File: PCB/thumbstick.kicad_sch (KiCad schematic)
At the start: 2 parts

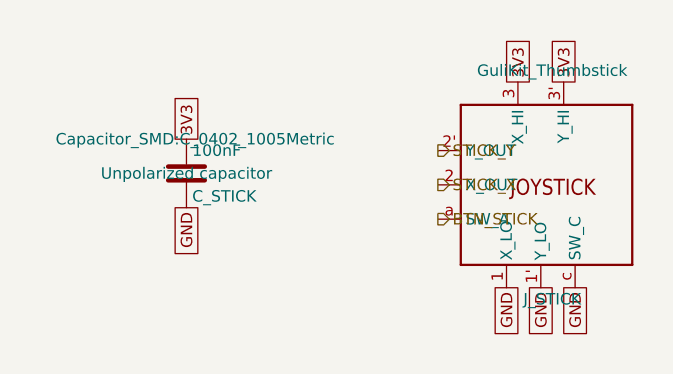
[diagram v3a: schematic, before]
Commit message: layout: everything is on the board
The board edge cuts are down to 100mm x 35mm. All the components have the right footprints and are on the board, but no traces exist yet, and not all circuits are laid out properly yet. Lots of DRC warnings.
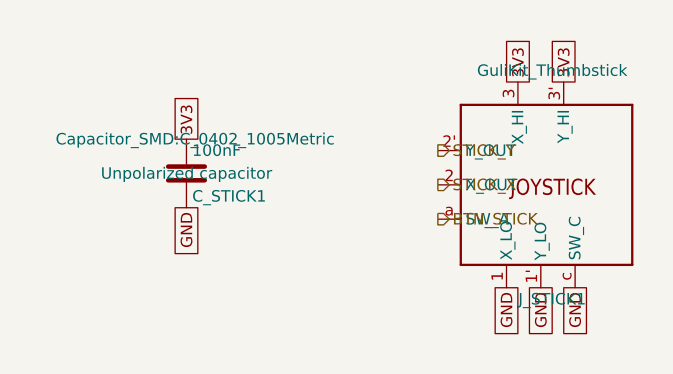
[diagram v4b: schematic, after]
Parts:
- removed C_STICK: 100nF, Capacitor_SMD:C_0402_1005Metric, symbol Device:C
- removed J_STICK: GuliKit_Thumbstick, SnipsControllers_Custom:GuliKit_HallStick, symbol SnipsControllers_Custom:GuliKit_HallStick
- added C_STICK1: 100nF, Capacitor_SMD:C_0402_1005Metric, symbol Device:C
- added J_STICK1: GuliKit_Thumbstick, SnipsControllers_Custom:GuliKit_HallStick, symbol SnipsControllers_Custom:GuliKit_HallStick
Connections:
- net 3V3: now also C_STICK1.1, J_STICK1.3 (X_HI), J_STICK1.3' (Y_HI)
- net BTN_STICK: now also J_STICK1.a (SW_A)
- net GND: now also C_STICK1.2, J_STICK1.1 (X_LO), J_STICK1.1' (Y_LO), J_STICK1.c (SW_C)
- net STICK_X: now also J_STICK1.2 (X_OUT)
- net STICK_Y: now also J_STICK1.2' (Y_OUT)
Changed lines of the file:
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@@
+		)
+	)
+	(global_label "3V3"
+		(shape passive)
+		(at 170.18 93.98 90)
+		(fields_autoplaced yes)
+		(effects
+			(font
+				(size 1.27 1.27)
+			)
+			(justify left)
+		)
+		(property "Intersheetrefs" "${INTERSHEET_REFS}"
+			(at 170.18 93.98 0)
+			(hide yes)
+			(show_name no)
+			(do_not_autoplace no)
+			(effects
+				(font
+					(size 1.27 1.27)
+				)
+			)
 		)
 	)
 	(global_label "GND"
 		(shape passive)
+		(at 163.83 116.84 270)
+		(fields_autoplaced yes)
+		(effects
+			(font
+				(size 1.27 1.27)
+			)
+			(justify right)
+		)
+		(property "Intersheetrefs" "${INTERSHEET_REFS}"
+			(at 163.83 116.84 0)
+			(hide yes)
+			(show_name no)
+			(do_not_autoplace no)
+			(effects
+				(font
+					(size 1.27 1.27)
+				)
+			)
+		)
+	)
+	(global_label "3V3"
+		(shape passive)
+		(at 128.27 100.33 90)
+		(fields_autoplaced yes)
+		(effects
+			(font
+				(size 1.27 1.27)
+			)
+			(justify left)
+		)
+		(property "Intersheetrefs" "${INTERSHEET_REFS}"
+			(at 128.27 100.33 0)
+			(hide yes)
+			(show_name no)
+			(do_not_autoplace no)
+			(effects
+				(font
+					(size 1.27 1.27)
+				)
+			)
+		)
+	)
+	(global_label "GND"
+		(shape passive)
 		(at 128.27 107.95 270)
 		(fields_autoplaced yes)
@@
 	(global_label "3V3"
 		(shape passive)
-		(at 170.18 93.98 90)
-		(fields_autoplaced yes)
-		(effects
-			(font
-				(size 1.27 1.27)
-			)
-			(justify left)
-		)
-		(property "Intersheetrefs" "${INTERSHEET_REFS}"
-			(at 170.18 93.98 0)
-			(hide yes)
-			(show_name no)
-			(do_not_autoplace no)
-			(effects
-				(font
-					(size 1.27 1.27)
-				)
-			)
-		)
-	)
-	(global_label "3V3"
-		(shape passive)
-		(at 128.27 100.33 90)
-		(fields_autoplaced yes)
-		(effects
-			(font
-				(size 1.27 1.27)
-			)
-			(justify left)
-		)
-		(property "Intersheetrefs" "${INTERSHEET_REFS}"
-			(at 128.27 100.33 0)
+		(at 165.1 93.98 90)
+		(fields_autoplaced yes)
+		(effects
+			(font
+				(size 1.27 1.27)
+			)
+			(justify left)
+		)
+		(property "Intersheetrefs" "${INTERSHEET_REFS}"
+			(at 165.1 93.98 0)
 			(hide yes)
 			(show_name no)
@@
 		)
 	)
-	(global_label "GND"
-		(shape passive)
-		(at 163.83 116.84 270)
-		(fields_autoplaced yes)
-		(effects
-			(font
-				(size 1.27 1.27)
-			)
-			(justify right)
-		)
-		(property "Intersheetrefs" "${INTERSHEET_REFS}"
-			(at 163.83 116.84 0)
-			(hide yes)
-			(show_name no)
-			(do_not_autoplace no)
-			(effects
-				(font
-					(size 1.27 1.27)
-				)
-			)
-		)
-	)
-	(global_label "3V3"
-		(shape passive)
-		(at 165.1 93.98 90)
-		(fields_autoplaced yes)
-		(effects
-			(font
-				(size 1.27 1.27)
-			)
-			(justify left)
-		)
-		(property "Intersheetrefs" "${INTERSHEET_REFS}"
-			(at 165.1 93.98 0)
-			(hide yes)
-			(show_name no)
-			(do_not_autoplace no)
-			(effects
-				(font
-					(size 1.27 1.27)
-				)
-			)
+	(hierarchical_label "STICK_Y"
+		(shape output)
+		(at 156.21 101.6 0)
+		(effects
+			(font
+				(size 1.27 1.27)
+			)
+			(justify left)
 		)
 	)
@@
 		)
 	)
-	(hierarchical_label "STICK_Y"
-		(shape output)
-		(at 156.21 101.6 0)
-		(effects
-			(font
-				(size 1.27 1.27)
-			)
-			(justify left)
+	(symbol
+		(lib_id "SnipsControllers_Custom:GuliKit_HallStick")
+		(at 168.91 105.41 0)
+		(unit 1)
+		(body_style 1)
+		(exclude_from_sim no)
+		(in_bom yes)
+		(on_board yes)
+		(in_pos_files yes)
+		(dnp no)
+		(fields_autoplaced yes)
+		(property "Reference" "J_STICK1"
+			(at 168.91 118.11 0)
+			(show_name no)
+			(do_not_autoplace no)
+			(effects
+				(font
+					(size 1.27 1.27)
+				)
+			)
+		)
+		(property "Value" "GuliKit_Thumbstick"
+			(at 168.91 92.71 0)
+			(show_name no)
+			(do_not_autoplace no)
+			(effects
+				(font
+					(size 1.27 1.27)
+				)
+			)
+		)
+		(property "Footprint" "SnipsControllers_Custom:GuliKit_HallStick"
+			(at 168.91 105.41 0)
+			(hide yes)
+			(show_name no)
+			(do_not_autoplace no)
+			(effects
+				(font
+					(size 1.27 1.27)
+				)
+			)
+		)
+		(property "Datasheet" ""
+			(at 168.91 105.41 0)
+			(hide yes)
+			(show_name no)
+			(do_not_autoplace no)
+			(effects
+				(font
+					(size 1.27 1.27)
+				)
+			)
+		)
+		(property "Description" "OEM-replacement-style hall/TMR analog thumbstick with center-push switch (ALPS RKJXV1224 / C&K THB001P footprint family). 2-axis potentiometer-emulation interface, not a simple VCC/GND/X/Y/SW breakout: pins 1/2/3 are the X axis low/wiper/high, pins 1'/2'/3' are the Y axis low/wiper/high, pins a/c are the switch (b/d are mechanically-redundant duplicate switch legs, intentionally unconnected). Drive 1 and 1' to GND, 3 and 3' to 3V3; read wipers 2 (X) and 2' (Y) on ADC pins; wire switch a to a GPIO and c to GND. Adapted from dbenoy/thumbstick-breakout (CC-BY-SA 4.0, Copyright (c) Daniel Benoy)."
+			(at 168.91 105.41 0)
+			(hide yes)
+			(show_name no)
+			(do_not_autoplace no)
+			(effects
+				(font
+					(size 1.27 1.27)
+				)
+			)
+		)
+		(pin "1"
+		)
+		(pin "1'"
+		)
+		(pin "2"
+		)
+		(pin "2'"
+		)
+		(pin "3"
+		)
+		(pin "3'"
+		)
+		(pin "a"
+		)
+		(pin "c"
+		)
+		(instances
+			(project "snips_controller"
+				(path "/21935953-32a0-46ad-8079-8177920c6978/346238e1-b4e6-4959-a557-1b480b53e730"
+					(reference "J_STICK1")
+					(unit 1)
+				)
+			)
 		)
 	)
@@
 		(dnp no)
 		(fields_autoplaced yes)
-		(property "Reference" "C_STICK"
+		(property "Reference" "C_STICK1"
 			(at 128.905 106.68 0)
 			(show_name no)
@@
 		(instances
 			(project "snips_controller"
-				(path "/f9d779c6-e1a6-4677-9004-6e9cc3d2fa8d/0d5246ec-5d9d-43ad-8a08-fe1da78eed54"
-					(reference "C_STICK")
+				(path "/21935953-32a0-46ad-8079-8177920c6978/346238e1-b4e6-4959-a557-1b480b53e730"
+					(reference "C_STICK1")
 					(unit 1)
 				)
-			)
-		)
-	)
-	(symbol
-		(lib_id "SnipsControllers_Custom:GuliKit_HallStick")
-		(at 168.91 105.41 0)
-		(unit 1)
-		(body_style 1)
-		(exclude_from_sim no)
-		(in_bom yes)
-		(on_board yes)
-		(in_pos_files yes)
-		(dnp no)
-		(fields_autoplaced yes)
-		(property "Reference" "J_STICK"
-			(at 168.91 118.11 0)
-			(show_name no)
-			(do_not_autoplace no)
-			(effects
-				(font
-					(size 1.27 1.27)
-				)
-			)
-		)
-		(property "Value" "GuliKit_Thumbstick"
-			(at 168.91 92.71 0)
-			(show_name no)
-			(do_not_autoplace no)
-			(effects
-				(font
-					(size 1.27 1.27)
-				)
-			)
-		)
-		(property "Footprint" "SnipsControllers_Custom:GuliKit_HallStick"
-			(at 168.91 105.41 0)
-			(hide yes)
-			(show_name no)
-			(do_not_autoplace no)
-			(effects
-				(font
-					(size 1.27 1.27)
-				)
-			)
-		)
-		(property "Datasheet" ""
-			(at 168.91 105.41 0)
-			(hide yes)
-			(show_name no)
-			(do_not_autoplace no)
-			(effects
-				(font
-					(size 1.27 1.27)
-				)
-			)
-		)
-		(property "Description" "OEM-replacement-style hall/TMR analog thumbstick with center-push switch (ALPS RKJXV1224 / C&K THB001P footprint family). 2-axis potentiometer-emulation interface, not a simple VCC/GND/X/Y/SW breakout: pins 1/2/3 are the X axis low/wiper/high, pins 1'/2'/3' are the Y axis low/wiper/high, pins a/c are the switch (b/d are mechanically-redundant duplicate switch legs, intentionally unconnected). Drive 1 and 1' to GND, 3 and 3' to 3V3; read wipers 2 (X) and 2' (Y) on ADC pins; wire switch a to a GPIO and c to GND. Adapted from dbenoy/thumbstick-breakout (CC-BY-SA 4.0, Copyright (c) Daniel Benoy)."
-			(at 168.91 105.41 0)
-			(hide yes)
-			(show_name no)
-			(do_not_autoplace no)
-			(effects
-				(font
-					(size 1.27 1.27)
-				)
-			)
-		)
-		(pin "1"
-		)
-		(pin "1'"
-		)
-		(pin "2"
-		)
-		(pin "2'"
-		)
-		(pin "3"
-		)
-		(pin "3'"
-		)
-		(pin "a"
-		)
-		(pin "c"
-		)
-		(instances
-			(project "snips_controller"
-				(path "/f9d779c6-e1a6-4677-9004-6e9cc3d2fa8d/0d5246ec-5d9d-43ad-8a08-fe1da78eed54"
-					(reference "J_STICK")
-					(unit 1)
-				)

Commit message: task: part number populated (#26)
kicad-happy run part 2 - MPN numbers populated
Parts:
- C_STICK1: MF (none) -> Yageo; Manufacturer_Part_Number (none) -> CC0402KRX7R9BB104
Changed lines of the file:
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@@
+			)
+		)
+		(property "MF" "Yageo" (at 0 0 0)
+			(effects
+				(font
+					(size 1.27 1.27)
+				)
+				(hide yes)
+			)
+		)
+		(property "Manufacturer_Part_Number" "CC0402KRX7R9BB104" (at 0 0 0)
+			(effects
+				(font
+					(size 1.27 1.27)
+				)
+				(hide yes)
 			)
 		)

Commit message: task: generate production files (#27)
* task: generate production files

We have wrapped up board validation. Gerbers are now generated. Logo generated. Good to go.

* refactor: added STAT2

It was worth adding and will give us more info during battery charging.
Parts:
- J_STICK1: now left out of the parts list
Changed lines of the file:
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@@
 		(body_style 1)
 		(exclude_from_sim no)
-		(in_bom yes)
+		(in_bom no)
 		(on_board yes)
 		(in_pos_files yes)
@@
 			)
 		)
-		(property "MF" "Yageo" (at 0 0 0)
+		(property "MF" "Yageo"
+			(at 0 0 0)
+			(hide yes)
+			(show_name no)
+			(do_not_autoplace no)
 			(effects
 				(font
 					(size 1.27 1.27)
 				)
-				(hide yes)
 			)
 		)
-		(property "Manufacturer_Part_Number" "CC0402KRX7R9BB104" (at 0 0 0)
+		(property "Manufacturer_Part_Number" "CC0402KRX7R9BB104"
+			(at 0 0 0)
+			(hide yes)
+			(show_name no)
+			(do_not_autoplace no)
 			(effects
 				(font
 					(size 1.27 1.27)
 				)
-				(hide yes)
 			)
 		)
